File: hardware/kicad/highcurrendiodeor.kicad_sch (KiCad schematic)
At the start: 9 parts, among them Q19 CSD18563Q5A, U32 SMBJ24A_C19077578, U33 LM5050MKX-1/NOPB, U34 SMBJ24A_C19077578

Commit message: starting erc check
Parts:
- C33, C34: footprint Capacitor_SMD:C_0603_1608Metric -> 5v rail sm-easyedapro:C0603
- R90, R91: footprint Resistor_SMD:R_0603_1608Metric -> 5v rail sm-easyedapro:R0603
- U33: footprint Package_TO_SOT_SMD:TSOT-23-6 -> 5v rail sm-easyedapro:TSOT-23-6_L2.9-W1.6-P0.95-LS2.8-BL
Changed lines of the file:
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@@
 			)
 		)
-		(property "Footprint" "Resistor_SMD:R_0603_1608Metric"
+		(property "Footprint" "5v rail sm-easyedapro:R0603"
 			(at 151.13 123.19 0)
 			(effects
@@
 			)
 		)
-		(property "Footprint" "Resistor_SMD:R_0603_1608Metric"
+		(property "Footprint" "5v rail sm-easyedapro:R0603"
 			(at 210.82 83.82 0)
 			(effects
@@
 			)
 		)
-		(property "Footprint" "Capacitor_SMD:C_0603_1608Metric"
+		(property "Footprint" "5v rail sm-easyedapro:C0603"
 			(at 135.89 86.36 0)
 			(effects
@@
 			)
 		)
-		(property "Description" ""
+		(property "Description" "Power symbol creates a global label with name \"GND\" , ground"
 			(at 151.13 129.54 0)
 			(effects
@@
 			)
 		)
-		(property "Footprint" "Package_TO_SOT_SMD:TSOT-23-6"
+		(property "Footprint" "5v rail sm-easyedapro:TSOT-23-6_L2.9-W1.6-P0.95-LS2.8-BL"
 			(at 165.1 97.79 0)
 			(effects
@@
 			)
 		)
-		(property "Footprint" "Capacitor_SMD:C_0603_1608Metric"
+		(property "Footprint" "5v rail sm-easyedapro:C0603"
 			(at 210.82 96.52 0)
 			(effects

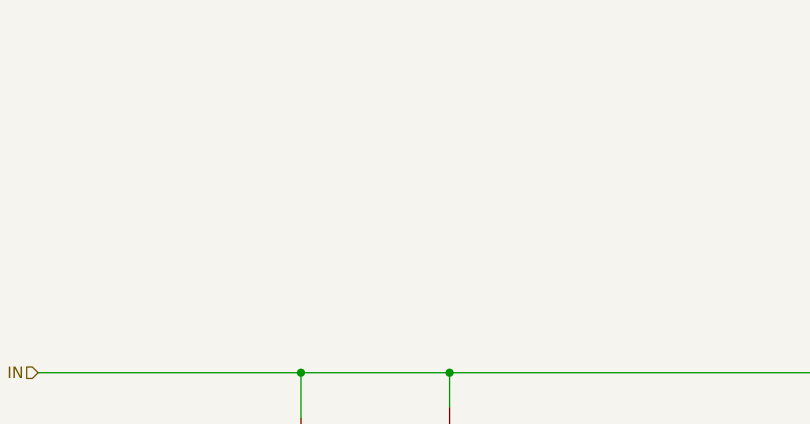
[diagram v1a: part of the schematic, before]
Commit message: prior switching to simpler ideal diode
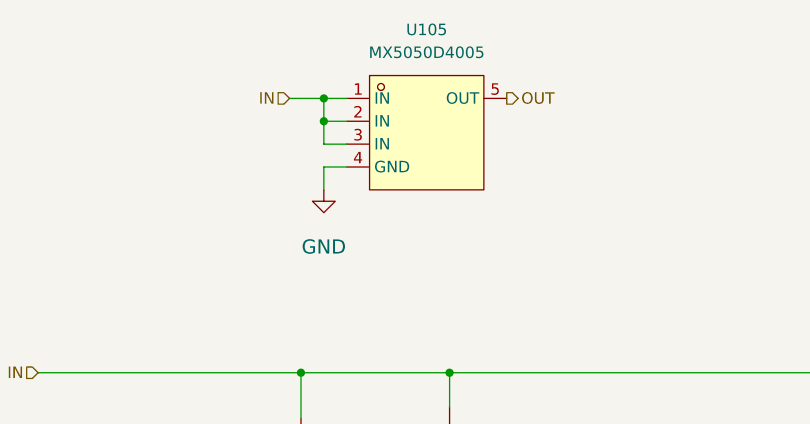
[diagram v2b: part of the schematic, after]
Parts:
- added U105: MX5050D4005, EasyEDA:TDSON-8_L5.9-W5.2-P1.27-BL-1, symbol EasyEDA:MX5050D4005
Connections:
- net GND: now also U105.4 (GND)
- net IN: now also U105.1 (IN), U105.2 (IN), U105.3 (IN)
- net OUT: now also U105.5 (OUT)

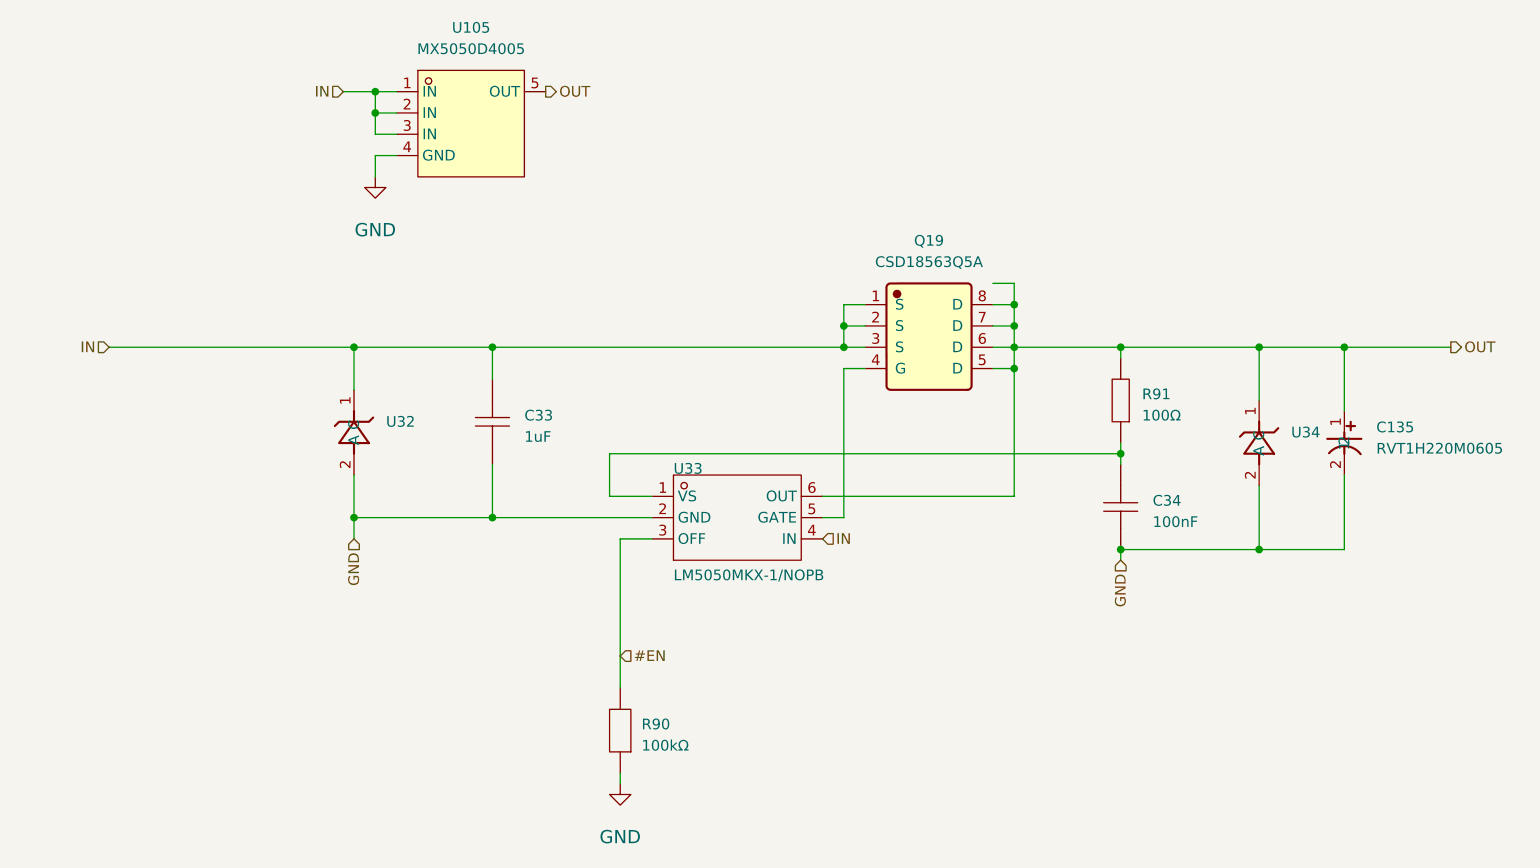
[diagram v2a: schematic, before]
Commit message: updated schematic to use simpler ideal diode
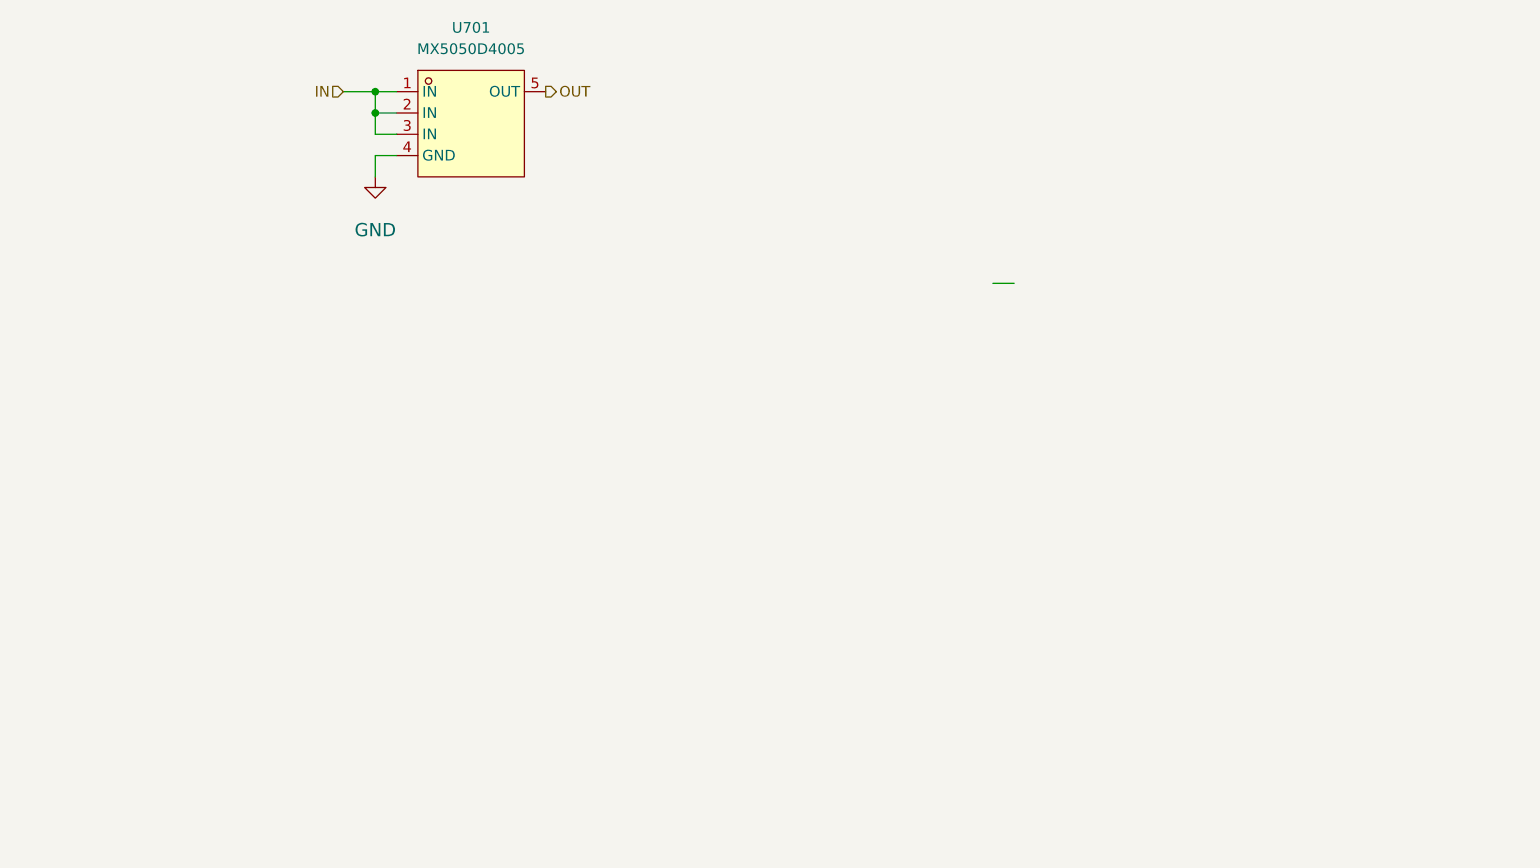
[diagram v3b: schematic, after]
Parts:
- removed C135: RVT1H220M0605, JLCImport:RVT1H220M0605, symbol JLCImport:RVT1H220M0605
- removed C33: 1uF, 5v rail sm-easyedapro:C0603, symbol 5v rail sm-easyedapro:CGA0603X5R105K500JT
- removed C34: 100nF, 5v rail sm-easyedapro:C0603, symbol 5v rail sm-easyedapro:CC0603KRX7R9BB104
- removed Q19: CSD18563Q5A, JLCImport:CSD18563Q5A, symbol JLCImport:CSD18563Q5A
- removed R90: 100kΩ, 5v rail sm-easyedapro:R0603, symbol 5v rail sm-easyedapro:FRC0603J104 TS
- removed R91: 100Ω, 5v rail sm-easyedapro:R0603, symbol 5v rail sm-easyedapro:0603WAF1000T5E
- removed U32, U34: SMBJ24A_C19077578, JLCImport:SMBJ24A_C19077578, symbol JLCImport:SMBJ24A_C19077578
- removed U33: LM5050MKX-1/NOPB, 5v rail sm-easyedapro:TSOT-23-6_L2.9-W1.6-P0.95-LS2.8-BL, symbol 5v rail sm-easyedapro:LM5050MKX-1/NOPB
- renumbered U105 to U701

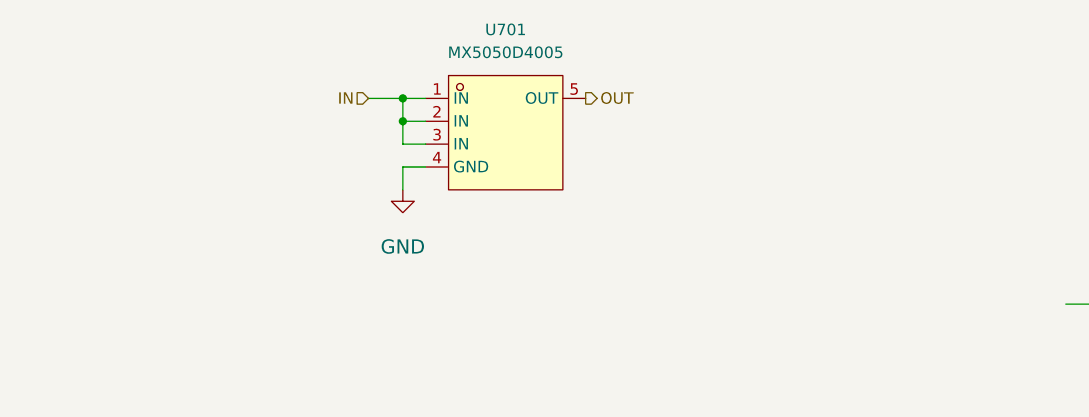
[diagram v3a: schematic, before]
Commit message: Update KiCad footprints and schematic placements
Convert and normalize multiple KiCad footprints and adjust schematic symbol placements. Upgraded EasyEDA and JLCImport footprints to modern pcbnew/footprint format (updated fp_line/pad primitives, uuids, embedded fonts/models), adjusted 3D model offsets, and expanded pad metadata. In schematics: moved EXB2HV102JV symbol position and added mirror Y, removed fields_autoplaced, set instance project path for U3201, and updated ServoConnectors port2 label to "sbus 3V". Also refreshed various PCB fp element UUIDs in svea_powerboard_rev3.kicad_pcb.
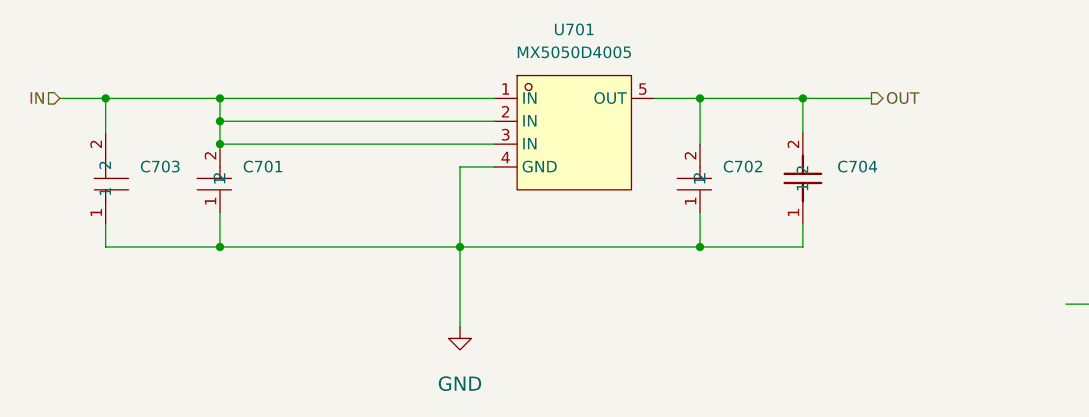
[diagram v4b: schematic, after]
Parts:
- added C701, C702: C0603C104K5RACAUTO, EasyEDA:C0603, symbol EasyEDA:C0603C104K5RACAUTO
- added C703: TCC1206X7R105M500HT, EasyEDA:C1206, symbol EasyEDA:TCC1206X7R105M500HT
- added C704: CL32B475KBUYNNE, JLCImport:CL32B475KBUYNNE, symbol JLCImport:CL32B475KBUYNNE
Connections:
- net GND: now also C701.1, C702.1, C703.1, C704.1
- net IN: now also C701.2, C703.2
- net OUT: now also C702.2, C704.2
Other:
- moved on the sheet: U701

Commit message: various updates
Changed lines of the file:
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@@
-	(wire
-		(pts
-			(xy 195.58 69.85) (xy 198.12 69.85)
-		)
-		(stroke
-			(width 0)
-			(type default)
-		)
-	)
 	(wire
 		(pts

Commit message: updating symbols to use kicad footprints where possible
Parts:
- C701, C702: footprint EasyEDA:C0603 -> Capacitor_SMD:C_0603_1608Metric
- C703: footprint EasyEDA:C1206 -> Capacitor_SMD:C_1206_3216Metric
- C704: footprint JLCImport:CL32B475KBUYNNE -> Capacitor_SMD:C_1210_3225Metric
- U701: footprint EasyEDA:TDSON-8_L5.9-W5.2-P1.27-BL-1 -> JLCImport:MX5050D4005
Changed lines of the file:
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@@
 			)
 		)
-		(property "Footprint" "EasyEDA:C0603"
+		(property "Footprint" "Capacitor_SMD:C_0603_1608Metric"
 			(at 109.22 60.96 0)
 			(effects
@@
 			)
 		)
-		(property "Footprint" "JLCImport:CL32B475KBUYNNE"
+		(property "Footprint" "Capacitor_SMD:C_1210_3225Metric"
 			(at 166.37 55.88 0)
 			(effects
@@
 			)
 		)
-		(property "Footprint" "EasyEDA:C0603"
+		(property "Footprint" "Capacitor_SMD:C_0603_1608Metric"
 			(at 162.56 60.96 0)
 			(effects
@@
 			)
 		)
-		(property "Footprint" "EasyEDA:TDSON-8_L5.9-W5.2-P1.27-BL-1"
+		(property "Footprint" "JLCImport:MX5050D4005"
 			(at 132.08 62.23 0)
 			(effects
@@
 			)
 		)
-		(property "Footprint" "EasyEDA:C1206"
+		(property "Footprint" "Capacitor_SMD:C_1206_3216Metric"
 			(at 91.44 68.58 0)
 			(effects

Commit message: updated more footprints
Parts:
- U701: footprint JLCImport:MX5050D4005 -> Package_TO_SOT_SMD:TDSON-8-1
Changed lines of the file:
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@@
 			)
 		)
-		(property "Footprint" "JLCImport:MX5050D4005"
+		(property "Footprint" "Package_TO_SOT_SMD:TDSON-8-1"
 			(at 132.08 62.23 0)
 			(effects
